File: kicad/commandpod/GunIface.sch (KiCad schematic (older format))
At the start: 3 parts

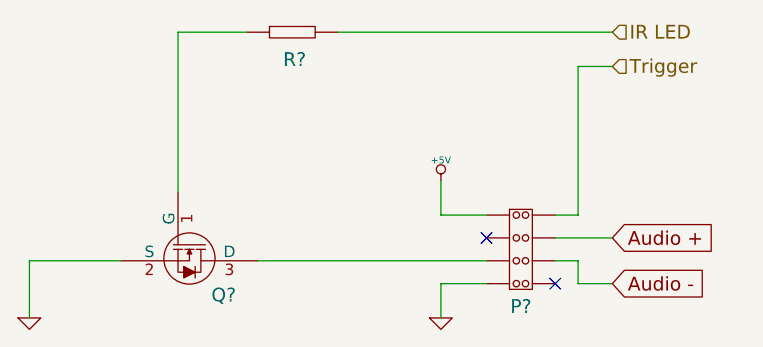
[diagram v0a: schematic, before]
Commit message: Annotated schematics
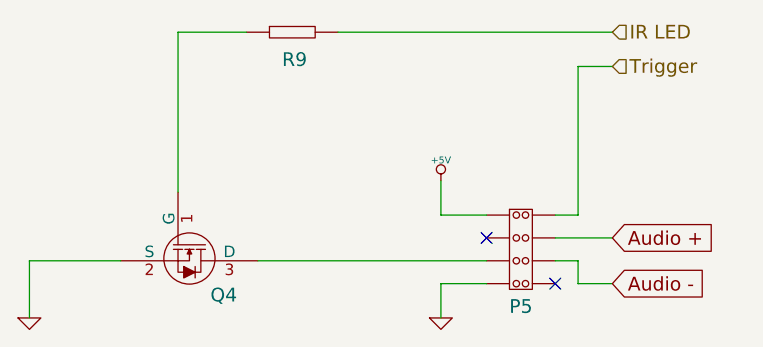
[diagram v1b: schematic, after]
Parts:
- gave numbers to parts that had none: 3
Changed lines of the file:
@@
 $EndDescr
 $Comp
-L GENERIC_RESISTOR R?
+L GENERIC_RESISTOR R9
 U 1 1 56D7F380
 P 5750 3550
-F 0 "R?" H 5760 3430 60  0000 C CNN
+F 0 "R9" H 5760 3430 60  0000 C CNN
 F 1 "GENERIC_RESISTOR" H 5790 3330 60  0001 C CNN
 F 2 "~" H 5700 3300 60  0000 C CNN
@@
 $EndComp
 $Comp
-L IRFML8244TRPBF Q?
+L IRFML8244TRPBF Q4
 U 1 1 56D7F387
 P 5300 4550
-F 0 "Q?" V 5450 4700 60  0000 C CNN
+F 0 "Q4" V 5450 4700 60  0000 C CNN
 F 1 "IRFML8244TRPBF" H 4550 4070 60  0001 C CNN
 F 2 "~" H 4500 4550 60  0000 C CNN
@@
 $EndComp
 $Comp
-L GND #PWR?
+L GND #PWR032
 U 1 1 56D7F38D
 P 4600 4800
-F 0 "#PWR?" H 4600 4800 30  0001 C CNN
+F 0 "#PWR032" H 4600 4800 30  0001 C CNN
 F 1 "GND" H 4600 4730 30  0001 C CNN
 F 2 "" H 4600 4800 60  0000 C CNN
@@
 $EndComp
 $Comp
-L HEADER_(8_WAY) P?
+L HEADER_(8_WAY) P5
 U 1 1 56D7F394
 P 6750 4450
-F 0 "P?" H 6750 4150 60  0000 C CNN
+F 0 "P5" H 6750 4150 60  0000 C CNN
 F 1 "HEADER_(8_WAY)" H 6750 4650 60  0001 C CNN
 F 2 "~" H 6800 4500 60  0000 C CNN
@@
 Audio -
 $Comp
-L GND #PWR?
+L GND #PWR033
 U 1 1 56D7F39E
 P 6400 4800
-F 0 "#PWR?" H 6400 4800 30  0001 C CNN
+F 0 "#PWR033" H 6400 4800 30  0001 C CNN
 F 1 "GND" H 6400 4730 30  0001 C CNN
 F 2 "" H 6400 4800 60  0000 C CNN
@@
 NoConn ~ 6900 4650
 $Comp
-L +5V #PWR?
+L +5V #PWR034
 U 1 1 56D7F3A6
 P 6400 4200
-F 0 "#PWR?" H 6400 4290 20  0001 C CNN
+F 0 "#PWR034" H 6400 4290 20  0001 C CNN
 F 1 "+5V" H 6400 4290 30  0000 C CNN
 F 2 "" H 6400 4200 60  0000 C CNN
